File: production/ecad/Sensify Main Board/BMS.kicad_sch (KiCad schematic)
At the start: 77 parts, among them J1 1-2834011-3, J2 1-2834011-2, Q1 2N700, Q2 PMPB13XNE,115, Q3 PMPB13XNE,115, Q4 BSS223PWH6327XTSA1, SW4 500ASSP3M2QE, U1 MAX17320G22, U2 BQ25306RTER, U3 LD29150DT33R, U4 LM22676MRX-5.0_NOPB

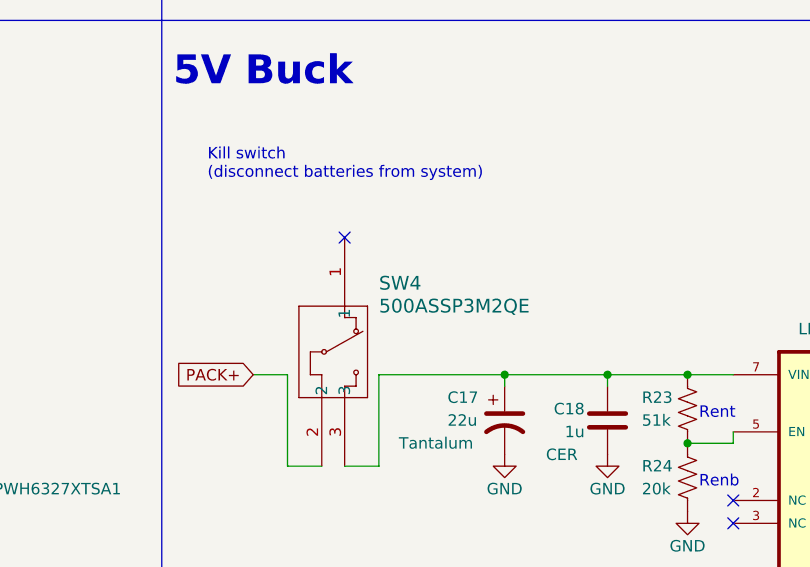
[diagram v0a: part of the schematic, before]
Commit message: smaller switch schematic edit
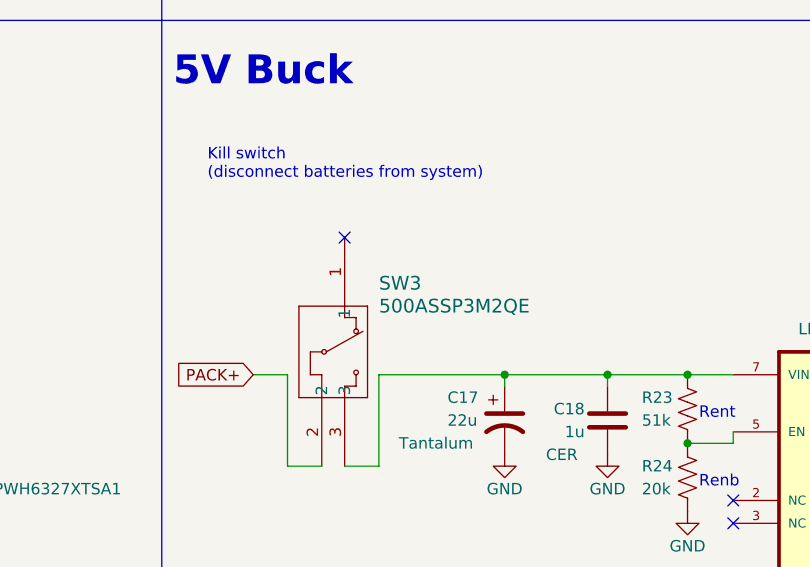
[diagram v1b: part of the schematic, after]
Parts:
- removed SW4: 500ASSP3M2QE, 500ASSP3M2QE_EWI, symbol BMS:500ASSP3M2QE
- added SW3: 500ASSP3M2QE, Sensify Footprints:500ASSP3M2QE_EWI, symbol BMS:500ASSP3M2QE
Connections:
- net PACK+: now also SW3.2
- net at C17.1, C18.1, R23.1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: now also SW3.3
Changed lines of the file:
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@@
-    )
-  )
-  (symbol (lib_id "BMS:500ASSP3M2QE") (at 255.27 90.17 270) (unit 1)
-    (in_bom yes) (on_board yes) (dnp no)
-    (property "Reference" "SW4" (at 259.08 95.25 90)
-      (effects (font (size 1.524 1.524)) (justify left))
-    )
-    (property "Value" "500ASSP3M2QE" (at 259.08 97.79 90)
-      (effects (font (size 1.524 1.524)) (justify left))
-    )
-    (property "Footprint" "500ASSP3M2QE_EWI" (at 255.27 90.17 0)
-      (effects (font (size 1.27 1.27) italic) hide)
-    )
-    (property "Datasheet" "500ASSP3M2QE" (at 255.27 90.17 0)
-      (effects (font (size 1.27 1.27) italic) hide)
-    )
-    (pin "1")
-    (pin "3")
-    (pin "2")
-    (instances
-      (project "Sensify Main Board"
-        (path "/9a7ba7c3-7d28-4a83-bdbc-38fbff59fcbe/13ad10b4-913e-414a-9863-b902179dcb8b"
-          (reference "SW4") (unit 1)
-        )
-      )
     )
   )
@@
         )
       )
+    )
+  )
+  (symbol (lib_id "BMS:500ASSP3M2QE") (at 255.27 90.17 270) (unit 1)
+    (in_bom yes) (on_board yes) (dnp no)
+    (property "Reference" "SW3" (at 259.08 95.25 90)
+      (effects (font (size 1.524 1.524)) (justify left))
+    )
+    (property "Value" "500ASSP3M2QE" (at 259.08 97.79 90)
+      (effects (font (size 1.524 1.524)) (justify left))
+    )
+    (property "Footprint" "Sensify Footprints:500ASSP3M2QE_EWI" (at 255.27 90.17 0)
+      (effects (font (size 1.27 1.27) italic) hide)
+    )
+    (property "Datasheet" "500ASSP3M2QE" (at 255.27 90.17 0)
+      (effects (font (size 1.27 1.27) italic) hide)
+    )
+    (pin "1")
+    (pin "3")
+    (pin "2")
+    (instances
+      (project "Sensify Main Board"
+        (path "/9a7ba7c3-7d28-4a83-bdbc-38fbff59fcbe/13ad10b4-913e-414a-9863-b902179dcb8b"
+          (reference "SW3") (unit 1)
+        )
+      )

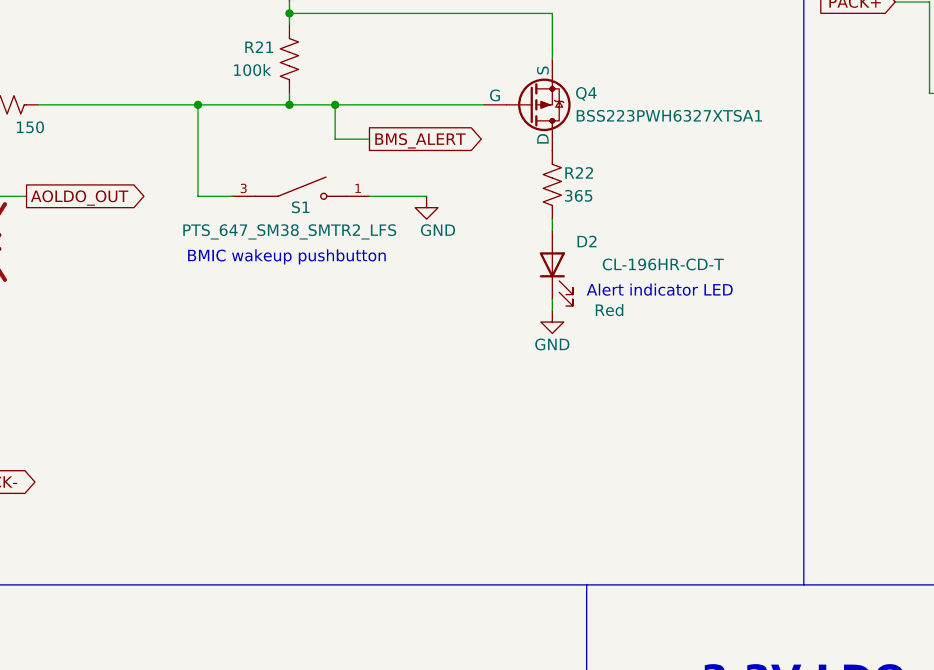
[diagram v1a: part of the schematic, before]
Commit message: smaller bms alert pushbutton +fixed reference designators + imu and haptics routing + tried to make stuff closer together
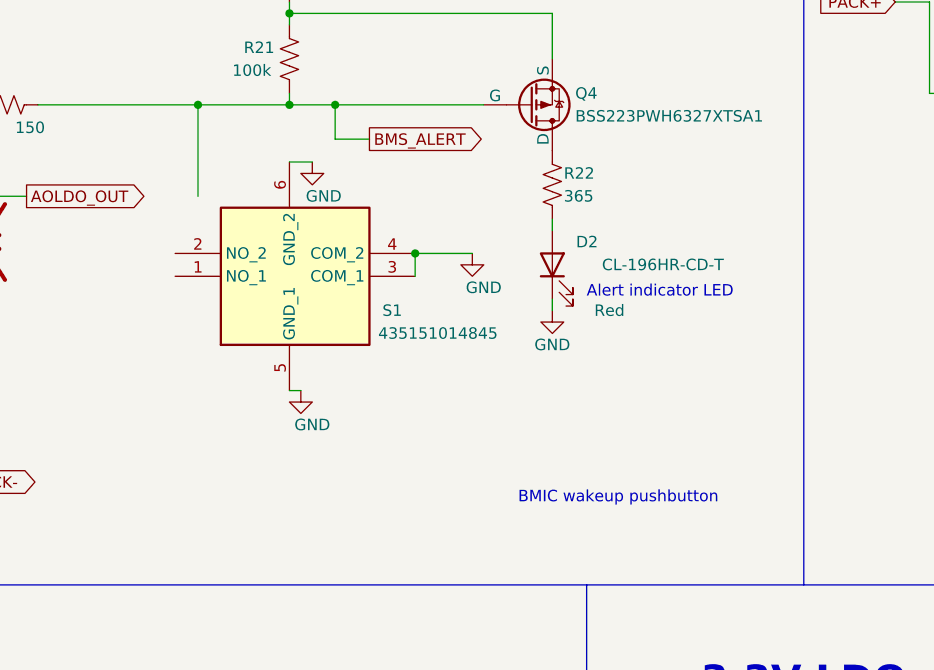
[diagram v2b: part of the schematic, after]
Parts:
- removed S1: PTS_647_SM38_SMTR2_LFS, Sensify Footprints:SW_PTS_647_SM38_SMTR2_LFS, symbol BMS:PTS_647_SM38_SMTR2_LFS
- added S1: 435151014845, 435151014845, symbol BMS:435151014845
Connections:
- net GND: now also S1.3 (COM_1), S1.4 (COM_2), S1.5 (GND_1), S1.6 (GND_2)
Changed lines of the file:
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@@
   (junction (at 271.78 200.66) (diameter 0) (color 0 0 0 0)
   )
+  (junction (at 191.77 133.35) (diameter 0) (color 0 0 0 0)
+  )
   (junction (at 44.45 124.46) (diameter 0) (color 0 0 0 0)
   )
@@
     (stroke (width 0) (type default))
   )
+  (wire (pts (xy 179.07 148.59) (xy 177.8 148.59))
+    (stroke (width 0) (type default))
+  )
   (wire (pts (xy 82.55 92.71) (xy 77.47 92.71))
     (stroke (width 0) (type default))
@@
     (stroke (width 0) (type default))
   )
-  (wire (pts (xy 186.69 127) (xy 193.04 127))
+  (wire (pts (xy 191.77 133.35) (xy 198.12 133.35))
     (stroke (width 0) (type default))
   )
@@
     (stroke (width 0) (type default))
   )
+  (wire (pts (xy 191.77 133.35) (xy 191.77 135.89))
+    (stroke (width 0) (type default))
+  )
   (wire (pts (xy 35.56 226.06) (xy 35.56 227.33))
     (stroke (width 0) (type default))
@@
     (stroke (width 0) (type default))
   )
+  (wire (pts (xy 177.8 123.19) (xy 180.34 123.19))
+    (stroke (width 0) (type default))
+  )
   (wire (pts (xy 182.88 120.65) (xy 182.88 116.84))
     (stroke (width 0) (type default))
@@
     (stroke (width 0) (type default))
   )
-  (wire (pts (xy 167.64 127) (xy 171.45 127))
-    (stroke (width 0) (type default))
-  )
   (wire (pts (xy 284.48 105.41) (xy 293.37 105.41))
     (stroke (width 0) (type default))
@@
     (effects (font (size 3.2 3.2) (thickness 0.6) bold) (justify left bottom))
   )
-  (text "BMIC wakeup pushbutton" (at 166.37 134.62 0)
+  (text "BMIC wakeup pushbutton" (at 203.2 161.29 0)
     (effects (font (size 1.27 1.27)) (justify left bottom))
   )
@@
     )
   )
+  (symbol (lib_id "BMS:435151014845") (at 180.34 148.59 90) (unit 1)
+    (in_bom yes) (on_board yes) (dnp no)
+    (property "Reference" "S1" (at 189.23 139.7 90)
+      (effects (font (size 1.27 1.27)))
+    )
+    (property "Value" "435151014845" (at 194.31 142.24 90)
+      (effects (font (size 1.27 1.27)))
+    )
+    (property "Footprint" "435151014845" (at 267.64 121.92 0)
+      (effects (font (size 1.27 1.27)) (justify left top) hide)
+    )
+    (property "Datasheet" "https://www.we-online.com/components/products/datasheet/435151014845.pdf" (at 367.64 121.92 0)
+      (effects (font (size 1.27 1.27)) (justify left top) hide)
+    )
+    (property "Height" "1.4" (at 567.64 121.92 0)
+      (effects (font (size 1.27 1.27)) (justify left top) hide)
+    )
+    (property "Manufacturer_Name" "Wurth Elektronik" (at 667.64 121.92 0)
+      (effects (font (size 1.27 1.27)) (justify left top) hide)
+    )
+    (property "Manufacturer_Part_Number" "435151014845" (at 767.64 121.92 0)
+      (effects (font (size 1.27 1.27)) (justify left top) hide)
+    )
+    (property "Mouser Part Number" "710-435151014845" (at 867.64 121.92 0)
+      (effects (font (size 1.27 1.27)) (justify left top) hide)
+    )
+    (property "Mouser Price/Stock" "https://www.mouser.co.uk/ProductDetail/Wurth-Elektronik/435151014845?qs=OlC7AqGiEDm1DeUERlpGng%3D%3D" (at 967.64 121.92 0)
+      (effects (font (size 1.27 1.27)) (justify left top) hide)
+    )
+    (property "Arrow Part Number" "" (at 1067.64 121.92 0)
+      (effects (font (size 1.27 1.27)) (justify left top) hide)
+    )
+    (property "Arrow Price/Stock" "" (at 1167.64 121.92 0)
+      (effects (font (size 1.27 1.27)) (justify left top) hide)
+    )
+    (pin "4")
+    (pin "5")
+    (pin "1")
+    (pin "6")
+    (pin "3")
+    (pin "2")
+    (instances
+      (project "Sensify Main Board"
+        (path "/9a7ba7c3-7d28-4a83-bdbc-38fbff59fcbe/13ad10b4-913e-414a-9863-b902179dcb8b"
+          (reference "S1") (unit 1)
+        )
+      )
+    )
+  )
   (symbol (lib_id "power:GND") (at 133.35 135.89 0) (unit 1)
     (in_bom yes) (on_board yes) (dnp no)
@@
     )
   )
-  (symbol (lib_id "power:GND") (at 193.04 127 0) (unit 1)
+  (symbol (lib_id "power:GND") (at 198.12 133.35 0) (unit 1)
     (in_bom yes) (on_board yes) (dnp no)
-    (property "Reference" "#PWR039" (at 193.04 133.35 0)
+    (property "Reference" "#PWR039" (at 198.12 139.7 0)
       (effects (font (size 1.27 1.27)) hide)
     )
-    (property "Value" "GND" (at 194.31 130.81 0)
+    (property "Value" "GND" (at 199.39 137.16 0)
       (effects (font (size 1.27 1.27)))
     )
-    (property "Footprint" "" (at 193.04 127 0)
+    (property "Footprint" "" (at 198.12 133.35 0)
       (effects (font (size 1.27 1.27)) hide)
     )
-    (property "Datasheet" "" (at 193.04 127 0)
+    (property "Datasheet" "" (at 198.12 133.35 0)
       (effects (font (size 1.27 1.27)) hide)
     )
@@
     )
   )
-  (symbol (lib_id "power:GND") (at 92.71 153.67 0) (unit 1)
+  (symbol (lib_id "power:GND") (at 180.34 123.19 0) (unit 1)
     (in_bom yes) (on_board yes) (dnp no)
-    (property "Reference" "#PWR024" (at 92.71 160.02 0)
+    (property "Reference" "#PWR084" (at 180.34 129.54 0)
       (effects (font (size 1.27 1.27)) hide)
     )
-    (property "Value" "GND" (at 92.71 157.48 0)
+    (property "Value" "GND" (at 181.61 127 0)
       (effects (font (size 1.27 1.27)))
     )
-    (property "Footprint" "" (at 92.71 153.67 0)
+    (property "Footprint" "" (at 180.34 123.19 0)
       (effects (font (size 1.27 1.27)) hide)
     )
-    (property "Datasheet" "" (at 92.71 153.67 0)
+    (property "Datasheet" "" (at 180.34 123.19 0)
       (effects (font (size 1.27 1.27)) hide)
     )
@@
       (project "Sensify Main Board"
         (path "/9a7ba7c3-7d28-4a83-bdbc-38fbff59fcbe/13ad10b4-913e-414a-9863-b902179dcb8b"
-          (reference "#PWR024") (unit 1)
-        )
-      )
-      (project "BMS"
-        (path "/b663df87-dd73-4614-b80d-e8e9f896eaba"
-          (reference "#PWR024") (unit 1)
+          (reference "#PWR084") (unit 1)
         )
       )
     )
   )
-  (symbol (lib_id "BMS:PTS_647_SM38_SMTR2_LFS") (at 179.07 127 0) (unit 1)
+  (symbol (lib_id "power:GND") (at 92.71 153.67 0) (unit 1)
     (in_bom yes) (on_board yes) (dnp no)
-    (property "Reference" "S1" (at 179.07 128.27 0)
-      (effects (font (size 1.27 1.27)))
+    (property "Reference" "#PWR024" (at 92.71 160.02 0)
+      (effects (font (size 1.27 1.27)) hide)
     )
-    (property "Value" "PTS_647_SM38_SMTR2_LFS" (at 177.8 130.81 0)
+    (property "Value" "GND" (at 92.71 157.48 0)
       (effects (font (size 1.27 1.27)))
     )
-    (property "Footprint" "Sensify Footprints:SW_PTS_647_SM38_SMTR2_LFS" (at 179.07 127 0)
-      (effects (font (size 1.27 1.27)) (justify bottom) hide)
-    )
-    (property "Datasheet" "https://www.ckswitches.com/media/2567/pts647.pdf" (at 179.07 127 0)
+    (property "Footprint" "" (at 92.71 153.67 0)
       (effects (font (size 1.27 1.27)) hide)
     )
-    (property "PARTREV" "11 Jun 19" (at 179.07 127 0)
-      (effects (font (size 1.27 1.27)) (justify bottom) hide)
-    )
-    (property "STANDARD" "Manufacturer Recommendations" (at 179.07 127 0)
-      (effects (font (size 1.27 1.27)) (justify bottom) hide)
-    )
-    (property "MAXIMUM_PACKAGE_HEIGHT" "3.8 mm" (at 179.07 127 0)
-      (effects (font (size 1.27 1.27)) (justify bottom) hide)
-    )
-    (property "MANUFACTURER" "C&K" (at 179.07 127 0)
-      (effects (font (size 1.27 1.27)) (justify bottom) hide)
+    (property "Datasheet" "" (at 92.71 153.67 0)
+      (effects (font (size 1.27 1.27)) hide)
     )
-    (pin "3")
     (pin "1")
     (instances
       (project "Sensify Main Board"
         (path "/9a7ba7c3-7d28-4a83-bdbc-38fbff59fcbe/13ad10b4-913e-414a-9863-b902179dcb8b"
-          (reference "S1") (unit 1)
+          (reference "#PWR024") (unit 1)
         )
       )
       (project "BMS"
         (path "/b663df87-dd73-4614-b80d-e8e9f896eaba"
-          (reference "S1") (unit 1)
+          (reference "#PWR024") (unit 1)
         )
       )
@@
         )
       )
+    )
+  )
+  (symbol (lib_id "power:GND") (at 179.07 148.59 0) (unit 1)
+    (in_bom yes) (on_board yes) (dnp no)
+    (property "Reference" "#PWR083" (at 179.07 154.94 0)
+      (effects (font (size 1.27 1.27)) hide)
+    )
+    (property "Value" "GND" (at 180.34 152.4 0)
+      (effects (font (size 1.27 1.27)))
+    )
+    (property "Footprint" "" (at 179.07 148.59 0)
+      (effects (font (size 1.27 1.27)) hide)
+    )
+    (property "Datasheet" "" (at 179.07 148.59 0)
+      (effects (font (size 1.27 1.27)) hide)
+    )
+    (pin "1")
+    (instances
+      (project "Sensify Main Board"
+        (path "/9a7ba7c3-7d28-4a83-bdbc-38fbff59fcbe/13ad10b4-913e-414a-9863-b902179dcb8b"
+          (reference "#PWR083") (unit 1)
+        )
+      )

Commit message: put in TPs + haptics half placed + tried to fit stuff in more
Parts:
- removed BAT2-_TP1: TestPoint, TestPoint:TestPoint_Pad_D1.5mm, symbol Connector:TestPoint
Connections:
- net BMS_ALERT: now also S1.1 (NO_1), S1.2 (NO_2)
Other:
- moved on the sheet: BMS_ALERT_TP1, PACK+_TP1
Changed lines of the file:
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@@
   (junction (at 182.88 116.84) (diameter 0) (color 0 0 0 0)
   )
+  (junction (at 165.1 133.35) (diameter 0) (color 0 0 0 0)
+  )
   (junction (at 284.48 105.41) (diameter 0) (color 0 0 0 0)
   )
@@
     (stroke (width 0) (type default))
   )
-  (wire (pts (xy 175.26 33.02) (xy 175.26 26.67))
-    (stroke (width 0) (type default))
-  )
   (wire (pts (xy 138.43 208.28) (xy 144.78 208.28))
     (stroke (width 0) (type default))
@@
     (stroke (width 0) (type default))
   )
+  (wire (pts (xy 165.1 133.35) (xy 165.1 127))
+    (stroke (width 0) (type default))
+  )
   (wire (pts (xy 62.23 133.35) (xy 62.23 135.89))
     (stroke (width 0) (type default))
@@
     (stroke (width 0) (type default))
   )
+  (wire (pts (xy 165.1 127) (xy 167.64 127))
+    (stroke (width 0) (type default))
+  )
   (wire (pts (xy 134.62 113.03) (xy 132.08 113.03))
     (stroke (width 0) (type default))
@@
     (stroke (width 0) (type default))
   )
+  (wire (pts (xy 165.1 135.89) (xy 165.1 133.35))
+    (stroke (width 0) (type default))
+  )
   (wire (pts (xy 21.59 30.48) (xy 26.67 30.48))
     (stroke (width 0) (type default))
@@
     (stroke (width 0) (type default))
   )
-  (wire (pts (xy 200.66 31.75) (xy 200.66 25.4))
+  (wire (pts (xy 170.18 46.99) (xy 170.18 40.64))
     (stroke (width 0) (type default))
   )
@@
     (stroke (width 0) (type default))
   )
-  (wire (pts (xy 175.26 46.99) (xy 175.26 40.64))
+  (wire (pts (xy 170.18 33.02) (xy 170.18 26.67))
     (stroke (width 0) (type default))
   )
@@
     )
   )
-  (global_label "BMS_ALERT" (shape input) (at 200.66 31.75 0) (fields_autoplaced)
+  (global_label "BMS_ALERT" (shape input) (at 170.18 46.99 0) (fields_autoplaced)
     (effects (font (size 1.27 1.27)) (justify left))
-    (property "Intersheetrefs" "${INTERSHEET_REFS}" (at 214.047 31.75 0)
+    (property "Intersheetrefs" "${INTERSHEET_REFS}" (at 183.567 46.99 0)
       (effects (font (size 1.27 1.27)) (justify left) hide)
     )
@@
     )
   )
-  (global_label "PACK+" (shape input) (at 175.26 46.99 0) (fields_autoplaced)
+  (global_label "PACK+" (shape input) (at 170.18 33.02 0) (fields_autoplaced)
     (effects (font (size 1.27 1.27)) (justify left))
-    (property "Intersheetrefs" "${INTERSHEET_REFS}" (at 184.7162 46.99 0)
+    (property "Intersheetrefs" "${INTERSHEET_REFS}" (at 179.6362 33.02 0)
       (effects (font (size 1.27 1.27)) (justify left) hide)
     )
@@
     )
   )
-  (global_label "BAT2-" (shape input) (at 175.26 33.02 0) (fields_autoplaced)
-    (effects (font (size 1.27 1.27)) (justify left))
-    (property "Intersheetrefs" "${INTERSHEET_REFS}" (at 184.3533 33.02 0)
-      (effects (font (size 1.27 1.27)) (justify left) hide)
-    )
-  )
   (hierarchical_label "SCL" (shape output) (at 71.12 30.48 0) (fields_autoplaced)
     (effects (font (size 1.27 1.27)) (justify left))
@@
     )
   )
-  (symbol (lib_id "Connector:TestPoint") (at 175.26 40.64 0) (unit 1)
+  (symbol (lib_id "Connector:TestPoint") (at 170.18 26.67 0) (unit 1)
     (in_bom yes) (on_board yes) (dnp no)
-    (property "Reference" "PACK+_TP1" (at 176.53 39.37 0)
+    (property "Reference" "PACK+_TP1" (at 171.45 25.4 0)
       (effects (font (size 1.27 1.27)) (justify left))
     )
-    (property "Value" "TestPoint" (at 176.53 42.672 0)
+    (property "Value" "TestPoint" (at 171.45 28.702 0)
       (effects (font (size 1.27 1.27)) (justify left))
     )
-    (property "Footprint" "TestPoint:TestPoint_Pad_D1.5mm" (at 180.34 40.64 0)
+    (property "Footprint" "TestPoint:TestPoint_Pad_D1.5mm" (at 175.26 26.67 0)
       (effects (font (size 1.27 1.27)) hide)
     )
-    (property "Datasheet" "~" (at 180.34 40.64 0)
+    (property "Datasheet" "~" (at 175.26 26.67 0)
       (effects (font (size 1.27 1.27)) hide)
     )
@@
     )
   )
-  (symbol (lib_id "Connector:TestPoint") (at 200.66 25.4 0) (unit 1)
+  (symbol (lib_id "Connector:TestPoint") (at 170.18 40.64 0) (unit 1)
     (in_bom yes) (on_board yes) (dnp no)
-    (property "Reference" "BMS_ALERT_TP1" (at 201.93 24.13 0)
+    (property "Reference" "BMS_ALERT_TP1" (at 171.45 39.37 0)
       (effects (font (size 1.27 1.27)) (justify left))
     )
-    (property "Value" "TestPoint" (at 201.93 27.432 0)
+    (property "Value" "TestPoint" (at 171.45 42.672 0)
       (effects (font (size 1.27 1.27)) (justify left))
     )
-    (property "Footprint" "TestPoint:TestPoint_Pad_D1.5mm" (at 205.74 25.4 0)
+    (property "Footprint" "TestPoint:TestPoint_Pad_D1.5mm" (at 175.26 40.64 0)
       (effects (font (size 1.27 1.27)) hide)
     )
-    (property "Datasheet" "~" (at 205.74 25.4 0)
+    (property "Datasheet" "~" (at 175.26 40.64 0)
       (effects (font (size 1.27 1.27)) hide)
     )
@@
         )
       )
-    )
-  )
-  (symbol (lib_id "Connector:TestPoint") (at 175.26 26.67 0) (unit 1)
-    (in_bom yes) (on_board yes) (dnp no)
-    (property "Reference" "BAT2-_TP1" (at 176.53 25.4 0)
-      (effects (font (size 1.27 1.27)) (justify left))
-    )
-    (property "Value" "TestPoint" (at 176.53 28.702 0)
-      (effects (font (size 1.27 1.27)) (justify left))
-    )
-    (property "Footprint" "TestPoint:TestPoint_Pad_D1.5mm" (at 180.34 26.67 0)
-      (effects (font (size 1.27 1.27)) hide)
-    )
-    (property "Datasheet" "~" (at 180.34 26.67 0)
-      (effects (font (size 1.27 1.27)) hide)
-    )
-    (pin "1")
-    (instances
-      (project "Sensify Main Board"
-        (path "/9a7ba7c3-7d28-4a83-bdbc-38fbff59fcbe/13ad10b4-913e-414a-9863-b902179dcb8b"
-          (reference "BAT2-_TP1") (unit 1)
-        )
-      )
-      (project "BMS"
-        (path "/b663df87-dd73-4614-b80d-e8e9f896eaba"
-          (reference "BAT2-_TP1") (unit 1)
-        )
-      )
